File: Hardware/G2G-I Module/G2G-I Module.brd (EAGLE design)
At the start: 13.1 x 12.8 mm, 4 parts, among them J1 GROVE-4P-2.0-3470130P1

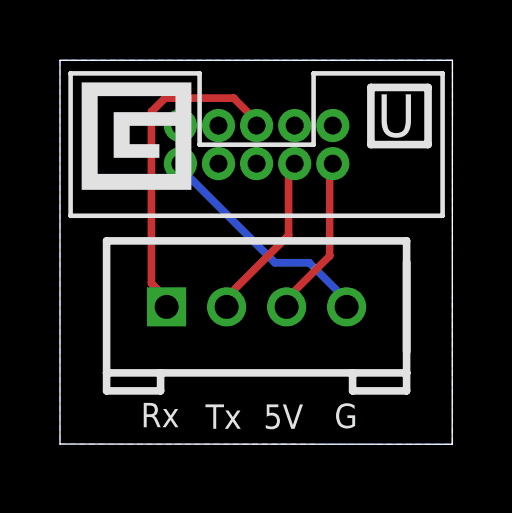
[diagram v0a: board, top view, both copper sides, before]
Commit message: Added G2G-A and G2G-I modules.
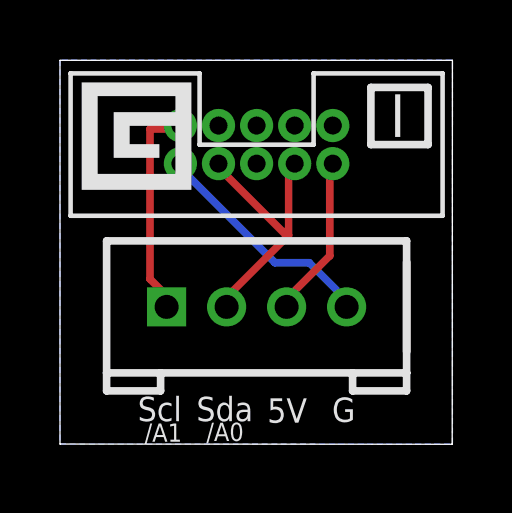
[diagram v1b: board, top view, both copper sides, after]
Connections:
- removed net RX: J1.1, U$1.5
- removed net TX: J1.2, U$1.4
- new net SCL: J1.1, U$1.9
- new net SDA: J1.2, U$1.8
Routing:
- net RX: track 10.9 -> 0.00 mm
- net SDA: track 0.00 -> 8.97 mm
- net SCL: track 0.00 -> 7.26 mm
- net TX: track 5.75 -> 0.00 mm
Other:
- board text added: "/A0"
- board text added: "/A1"
- board text added: "G2G-I"
- board text added: "I"
- board text added: "Scl"
- board text added: "Sda"
- board text removed: "G2G-U"
- board text removed: "Rx"
- board text removed: "Tx"
- board text removed: "U"
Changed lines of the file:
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@@
 <wire x1="13.0812" y1="12.7916" x2="0" y2="12.7916" width="0" layer="20"/>
 <wire x1="0" y1="12.7916" x2="0" y2="0" width="0" layer="20"/>
-<text x="10.5664" y="10.2362" size="1.4224" layer="21">U</text>
+<text x="10.9982" y="10.2362" size="1.4224" layer="21" font="vector">I</text>
 <wire x1="10.3632" y1="11.8872" x2="10.3632" y2="9.9822" width="0.254" layer="21"/>
 <wire x1="10.3632" y1="9.9822" x2="12.2682" y2="9.9822" width="0.254" layer="21"/>
 <wire x1="12.2682" y1="9.9822" x2="12.2682" y2="11.8872" width="0.254" layer="21"/>
 <wire x1="12.2682" y1="11.8872" x2="10.3632" y2="11.8872" width="0.254" layer="21"/>
-<text x="12.5476" y="1.905" size="1.016" layer="22" rot="MR0">G2G-U</text>
+<text x="12.5222" y="1.905" size="1.016" layer="22" rot="MR0">G2G-I</text>
 <text x="12.5222" y="0.6096" size="1.016" layer="22" rot="MR0">v1.0</text>
-<text x="2.6924" y="0.5588" size="0.8128" layer="21">Rx</text>
-<text x="4.8514" y="0.508" size="0.8128" layer="21">Tx</text>
-<text x="6.7818" y="0.508" size="0.8128" layer="21">5V</text>
-<text x="9.144" y="0.5334" size="0.8128" layer="21">G</text>
-<text x="12.5984" y="5.7912" size="1.4224" layer="22" rot="MR0">Gadgeteer.in'</text>
+<text x="2.5908" y="0.762" size="0.8128" layer="21">Scl</text>
+<text x="4.5466" y="0.762" size="0.8128" layer="21">Sda</text>
+<text x="6.9088" y="0.7112" size="0.8128" layer="21">5V</text>
+<text x="9.0678" y="0.7366" size="0.8128" layer="21">G</text>
+<text x="12.6238" y="5.7658" size="1.4224" layer="22" rot="MR0">Gadgeteer.in'</text>
 <rectangle x1="0.7225" y1="8.4731" x2="4.3801" y2="8.5493" layer="21"/>
 <rectangle x1="0.7225" y1="8.5493" x2="4.3801" y2="8.6255" layer="21"/>
@@
 <rectangle x1="0.7225" y1="11.9021" x2="4.3801" y2="11.9783" layer="21"/>
 <rectangle x1="0.7225" y1="11.9783" x2="4.3801" y2="12.0545" layer="21"/>
+<text x="4.8768" y="0.1016" size="0.6096" layer="21">/A0</text>
+<text x="2.8194" y="0.0762" size="0.6096" layer="21">/A1</text>
 </plain>
 <attributes>
@@
 </elements>
 <signals>
-<signal name="TX">
-<contactref element="U$1" pad="4"/>
-<contactref element="J1" pad="2"/>
-<wire x1="7.62" y1="6.9596" x2="7.62" y2="9.2456" width="0.254" layer="1"/>
-<wire x1="5.5626" y1="4.9022" x2="7.62" y2="6.9596" width="0.254" layer="1"/>
-<wire x1="7.62" y1="9.2456" x2="7.8232" y2="9.3472" width="0.254" layer="1"/>
-<wire x1="5.5626" y1="4.9022" x2="5.5532" y2="4.572" width="0.254" layer="1"/>
-</signal>
-<signal name="RX">
-<contactref element="U$1" pad="5"/>
-<contactref element="J1" pad="1"/>
-<wire x1="6.477" y1="10.8458" x2="6.477" y2="10.6172" width="0.254" layer="1"/>
-<wire x1="5.7912" y1="11.5316" x2="6.477" y2="10.8458" width="0.254" layer="1"/>
-<wire x1="3.5052" y1="11.5316" x2="5.7912" y2="11.5316" width="0.254" layer="1"/>
-<wire x1="3.048" y1="11.0744" x2="3.5052" y2="11.5316" width="0.254" layer="1"/>
-<wire x1="3.048" y1="5.3594" x2="3.048" y2="11.0744" width="0.254" layer="1"/>
-<wire x1="3.5052" y1="4.9022" x2="3.048" y2="5.3594" width="0.254" layer="1"/>
-<wire x1="6.477" y1="10.6172" x2="6.5532" y2="10.6172" width="0.254" layer="1"/>
-<wire x1="3.5052" y1="4.9022" x2="3.5532" y2="4.572" width="0.254" layer="1"/>
-</signal>
 <signal name="GND">
 <contactref element="U$1" pad="10"/>
@@
 <wire x1="7.62" y1="4.9022" x2="7.5532" y2="4.572" width="0.254" layer="1"/>
 </signal>
+<signal name="SDA">
+<contactref element="U$1" pad="8"/>
+<contactref element="J1" pad="2"/>
+<wire x1="7.62" y1="6.9596" x2="7.62" y2="9.2456" width="0.254" layer="1"/>
+<wire x1="5.5626" y1="4.9022" x2="7.5802" y2="6.9198" width="0.254" layer="1"/>
+<wire x1="7.5802" y1="6.9198" x2="7.62" y2="6.9596" width="0.254" layer="1"/>
+<wire x1="5.4864" y1="4.8006" x2="5.4864" y2="4.572" width="0.254" layer="1"/>
+<wire x1="5.4864" y1="4.572" x2="5.5532" y2="4.572" width="0.254" layer="1"/>
+<wire x1="5.4864" y1="4.8006" x2="5.5626" y2="4.9022" width="0.254" layer="1"/>
+<wire x1="7.5802" y1="6.9198" x2="5.5" y2="9" width="0.254" layer="1"/>
+<wire x1="5.5" y1="9" x2="5.2832" y2="9.3472" width="0.254" layer="1"/>
+</signal>
+<signal name="SCL">
+<contactref element="J1" pad="1"/>
+<contactref element="U$1" pad="9"/>
+<wire x1="3" y1="10.5" x2="4" y2="10.5" width="0.254" layer="1"/>
+<wire x1="3" y1="5.5" x2="3" y2="10.5" width="0.254" layer="1"/>
+<wire x1="3.5" y1="5" x2="3" y2="5.5" width="0.254" layer="1"/>
+<wire x1="4" y1="10.5" x2="4.0132" y2="10.6172" width="0.254" layer="1"/>
+<wire x1="3.5" y1="5" x2="3.5532" y2="4.572" width="0.254" layer="1"/>
+</signal>
 </signals>

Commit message: Passed Seeed Studio dru tests.
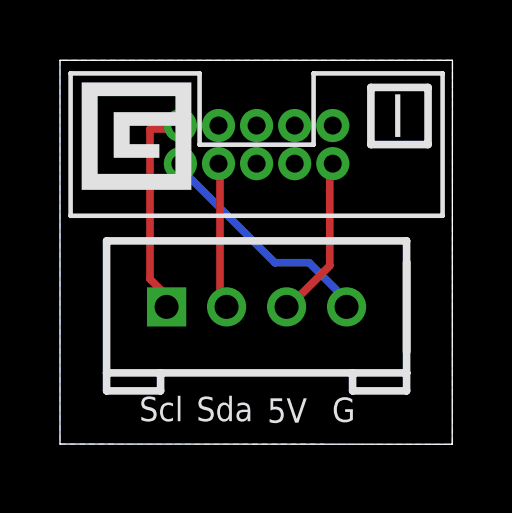
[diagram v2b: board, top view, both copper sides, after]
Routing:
- net SDA: track 8.97 -> 4.93 mm
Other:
- board text removed: "/A0"
- board text removed: "/A1"
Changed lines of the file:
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@@
 <text x="12.5222" y="1.905" size="1.016" layer="22" rot="MR0">G2G-I</text>
 <text x="12.5222" y="0.6096" size="1.016" layer="22" rot="MR0">v1.0</text>
-<text x="2.5908" y="0.762" size="0.8128" layer="21">Scl</text>
+<text x="2.6416" y="0.762" size="0.8128" layer="21">Scl</text>
 <text x="4.5466" y="0.762" size="0.8128" layer="21">Sda</text>
 <text x="6.9088" y="0.7112" size="0.8128" layer="21">5V</text>
@@
 <rectangle x1="0.7225" y1="11.9021" x2="4.3801" y2="11.9783" layer="21"/>
 <rectangle x1="0.7225" y1="11.9783" x2="4.3801" y2="12.0545" layer="21"/>
-<text x="4.8768" y="0.1016" size="0.6096" layer="21">/A0</text>
-<text x="2.8194" y="0.0762" size="0.6096" layer="21">/A1</text>
 </plain>
 <attributes>
@@
 </class>
 </classes>
-<designrules name="default">
+<designrules name="SeeedStudio_2layer_DRU_no_angle_20140221">
 <description language="de">&lt;b&gt;EAGLE Design Rules&lt;/b&gt;
 &lt;p&gt;
@@
 necessary adjustments and save your customized
 design rules under a new name.</description>
+<description language="zh">&lt;b&gt;Seeed Studio EAGLE Design Rules&lt;/b&gt;
+</description>
 <param name="layerSetup" value="(1*16)"/>
-<param name="mtCopper" value="0.035mm 0.035mm 0.035mm 0.035mm 0.035mm 0.035mm 0.035mm 0.035mm 0.035mm 0.035mm 0.035mm 0.035mm 0.035mm 0.035mm 0.035mm 0.035mm"/>
-<param name="mtIsolate" value="1.5mm 0.15mm 0.2mm 0.15mm 0.2mm 0.15mm 0.2mm 0.15mm 0.2mm 0.15mm 0.2mm 0.15mm 0.2mm 0.15mm 0.2mm"/>
-<param name="mdWireWire" value="8mil"/>
-<param name="mdWirePad" value="8mil"/>
-<param name="mdWireVia" value="8mil"/>
-<param name="mdPadPad" value="8mil"/>
-<param name="mdPadVia" value="8mil"/>
-<param name="mdViaVia" value="8mil"/>
-<param name="mdSmdPad" value="8mil"/>
-<param name="mdSmdVia" value="8mil"/>
-<param name="mdSmdSmd" value="8mil"/>
+<param name="mtCopper" value="0.035mm 0.0175mm 0.035mm 0.035mm 0.035mm 0.035mm 0.035mm 0.035mm 0.035mm 0.035mm 0.035mm 0.035mm 0.035mm 0.035mm 0.0175mm 0.035mm"/>
+<param name="mtIsolate" value="1.5mm 1.1mm 0.2mm 0.15mm 0.2mm 0.15mm 0.2mm 0.15mm 0.2mm 0.15mm 0.2mm 0.15mm 0.2mm 0.15mm 0.2mm"/>
+<param name="mdWireWire" value="6mil"/>
+<param name="mdWirePad" value="6mil"/>
+<param name="mdWireVia" value="6mil"/>
+<param name="mdPadPad" value="6mil"/>
+<param name="mdPadVia" value="6mil"/>
+<param name="mdViaVia" value="6mil"/>
+<param name="mdSmdPad" value="0mil"/>
+<param name="mdSmdVia" value="0mil"/>
+<param name="mdSmdSmd" value="0mil"/>
 <param name="mdViaViaSameLayer" value="8mil"/>
 <param name="mnLayersViaInSmd" value="2"/>
-<param name="mdCopperDimension" value="40mil"/>
-<param name="mdDrill" value="8mil"/>
+<param name="mdCopperDimension" value="10mil"/>
+<param name="mdDrill" value="10mil"/>
 <param name="mdSmdStop" value="0mil"/>
-<param name="msWidth" value="10mil"/>
-<param name="msDrill" value="24mil"/>
-<param name="msMicroVia" value="9.99mm"/>
+<param name="msWidth" value="6mil"/>
+<param name="msDrill" value="12mil"/>
+<param name="msMicroVia" value="12mil"/>
 <param name="msBlindViaRatio" value="0.5"/>
 <param name="rvPadTop" value="0.25"/>
@@
 <param name="rlMinPadBottom" value="10mil"/>
 <param name="rlMaxPadBottom" value="20mil"/>
-<param name="rlMinViaOuter" value="8mil"/>
+<param name="rlMinViaOuter" value="6mil"/>
 <param name="rlMaxViaOuter" value="20mil"/>
-<param name="rlMinViaInner" value="8mil"/>
+<param name="rlMinViaInner" value="6mil"/>
 <param name="rlMaxViaInner" value="20mil"/>
 <param name="rlMinMicroViaOuter" value="4mil"/>
@@
 <param name="psTop" value="-1"/>
 <param name="psBottom" value="-1"/>
-<param name="psFirst" value="-1"/>
+<param name="psFirst" value="0"/>
 <param name="psElongationLong" value="100"/>
 <param name="psElongationOffset" value="100"/>
 <param name="mvStopFrame" value="1"/>
 <param name="mvCreamFrame" value="0"/>
-<param name="mlMinStopFrame" value="4mil"/>
-<param name="mlMaxStopFrame" value="4mil"/>
+<param name="mlMinStopFrame" value="2mil"/>
+<param name="mlMaxStopFrame" value="2mil"/>
 <param name="mlMinCreamFrame" value="0mil"/>
 <param name="mlMaxCreamFrame" value="0mil"/>
-<param name="mlViaStopLimit" value="0mil"/>
+<param name="mlViaStopLimit" value="100mil"/>
 <param name="srRoundness" value="0"/>
 <param name="srMinRoundness" value="0mil"/>
@@
 <param name="checkAngle" value="0"/>
 <param name="checkFont" value="1"/>
-<param name="checkRestrict" value="1"/>
+<param name="checkRestrict" value="0"/>
 <param name="useDiameter" value="13"/>
 <param name="maxErrors" value="50"/>
@@
 <contactref element="J1" pad="3"/>
 <contactref element="U$1" pad="2"/>
-<wire x1="8.9916" y1="6.2738" x2="8.9916" y2="9.2456" width="0.254" layer="1"/>
-<wire x1="7.62" y1="4.9022" x2="8.9916" y2="6.2738" width="0.254" layer="1"/>
-<wire x1="8.9916" y1="9.2456" x2="9.0932" y2="9.3472" width="0.254" layer="1"/>
-<wire x1="7.62" y1="4.9022" x2="7.5532" y2="4.572" width="0.254" layer="1"/>
+<wire x1="8.9916" y1="5.9436" x2="8.9916" y2="9.2964" width="0.254" layer="1"/>
+<wire x1="7.62" y1="4.572" x2="8.9916" y2="5.9436" width="0.254" layer="1"/>
+<wire x1="8.9916" y1="9.2964" x2="9.0932" y2="9.3472" width="0.1524" layer="1"/>
+<wire x1="7.62" y1="4.572" x2="7.5532" y2="4.572" width="0.1524" layer="1"/>
 </signal>
 <signal name="SDA">
 <contactref element="U$1" pad="8"/>
 <contactref element="J1" pad="2"/>
-<wire x1="7.62" y1="6.9596" x2="7.62" y2="9.2456" width="0.254" layer="1"/>
-<wire x1="5.5626" y1="4.9022" x2="7.5802" y2="6.9198" width="0.254" layer="1"/>
-<wire x1="7.5802" y1="6.9198" x2="7.62" y2="6.9596" width="0.254" layer="1"/>
-<wire x1="5.4864" y1="4.8006" x2="5.4864" y2="4.572" width="0.254" layer="1"/>
-<wire x1="5.4864" y1="4.572" x2="5.5532" y2="4.572" width="0.254" layer="1"/>
-<wire x1="5.4864" y1="4.8006" x2="5.5626" y2="4.9022" width="0.254" layer="1"/>
-<wire x1="7.5802" y1="6.9198" x2="5.5" y2="9" width="0.254" layer="1"/>
-<wire x1="5.5" y1="9" x2="5.2832" y2="9.3472" width="0.254" layer="1"/>
+<wire x1="5.334" y1="4.7244" x2="5.334" y2="9.2964" width="0.254" layer="1"/>
+<wire x1="5.4864" y1="4.572" x2="5.334" y2="4.7244" width="0.1524" layer="1"/>
+<wire x1="5.334" y1="9.2964" x2="5.2832" y2="9.3472" width="0.1524" layer="1"/>
+<wire x1="5.4864" y1="4.572" x2="5.5532" y2="4.572" width="0.1524" layer="1"/>
 </signal>
 <signal name="SCL">
